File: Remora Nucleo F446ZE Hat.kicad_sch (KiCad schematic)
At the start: 16 parts, among them J1 NucleoF446ZE CN11 Header, J2 NucleoF446ZE CN12 Header, J3 UART_TX, J4 MSD-1-A

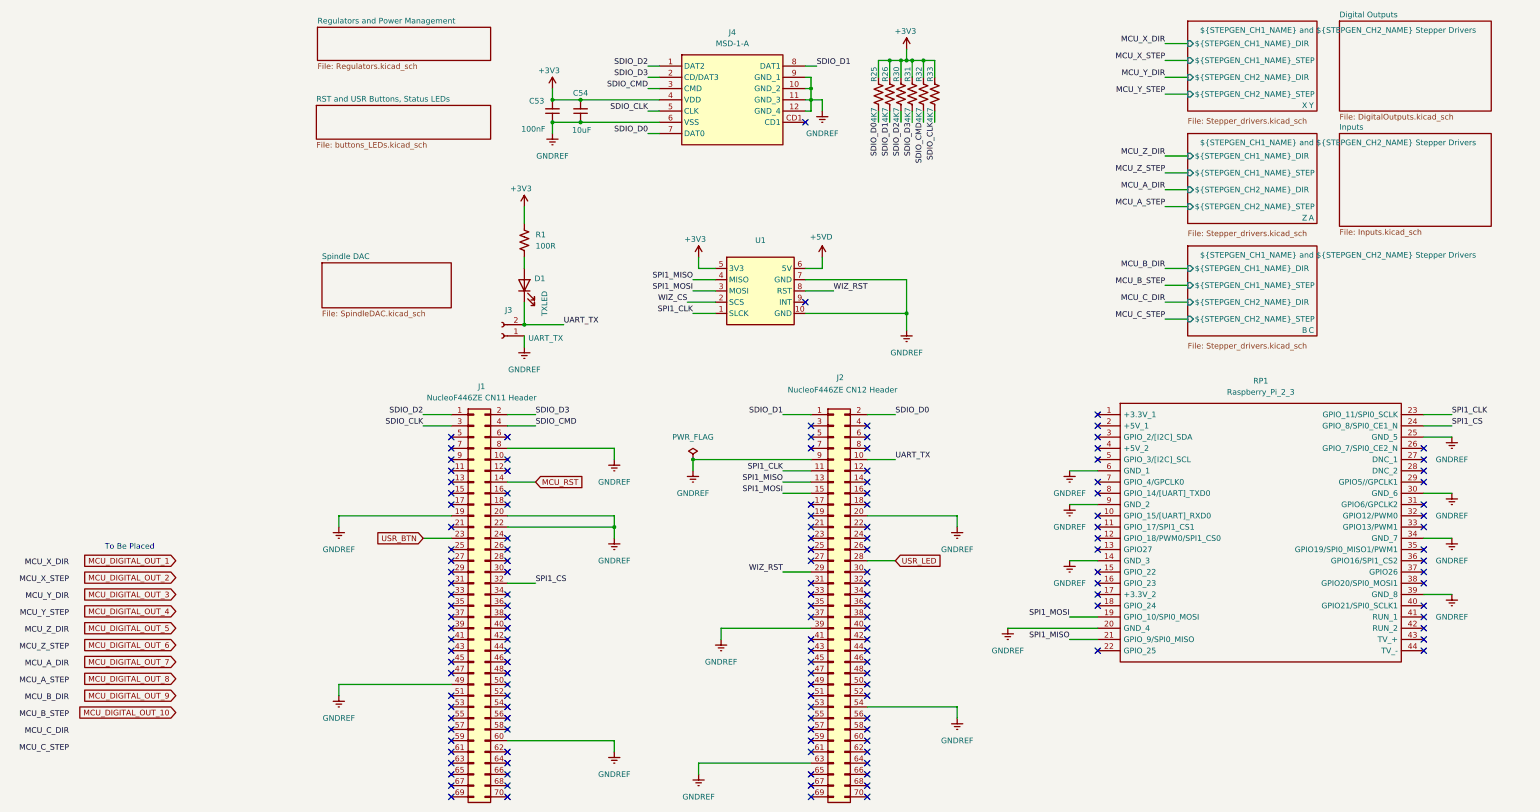
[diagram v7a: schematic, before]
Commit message: updates to read me, marked V1 parts inactive and made start on board layout for initial test board. fixes to BOM to suit
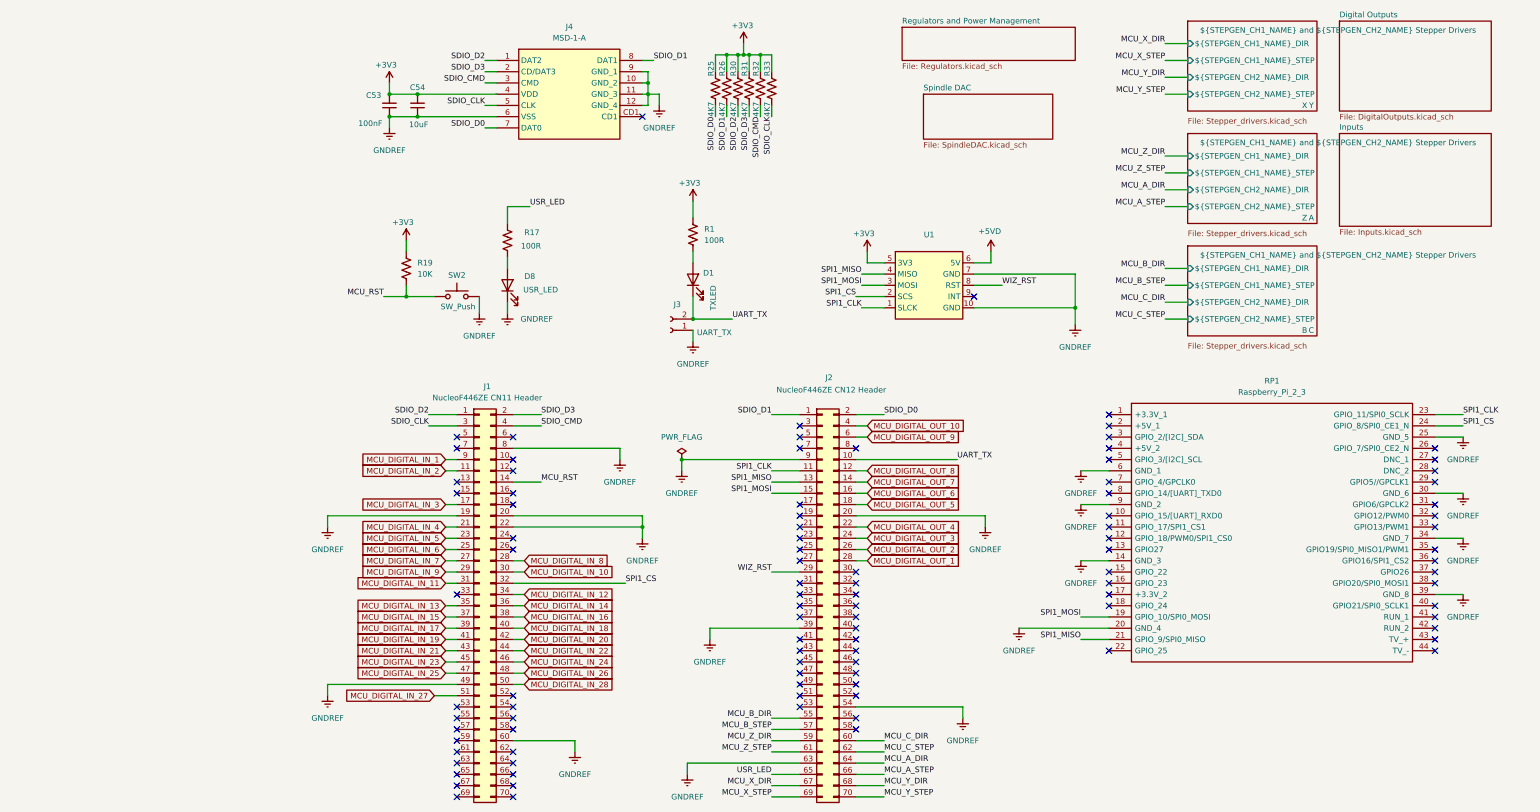
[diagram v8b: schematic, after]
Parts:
- added D8: USR_LED, Diode_SMD:D_1206_3216Metric_Pad1.42x1.75mm_HandSolder, symbol Device:LED
- added R17: 100R, Resistor_SMD:R_1206_3216Metric_Pad1.30x1.75mm_HandSolder, symbol Device:R_US
- added R19: 10K, Resistor_SMD:R_1206_3216Metric_Pad1.30x1.75mm_HandSolder, symbol Device:R_US
- added SW2: SW_Push, Button_Switch_SMD:SW_SPST_Omron_B3FS-100xP, symbol Switch:SW_Push
- J3: footprint EBWA_02_A:ADAMTECH_EBWA-02-A -> Connector_PinHeader_2.54mm:PinHeader_1x02_P2.54mm_Vertical
- RP1: footprint RPI3FootPrint:raspberrypi_2_3 -> RASPBERRYPI
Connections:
- net WIZ_CS is gone; now on net SPI1_CS: U1.2 (SCS)
- net +3V3: now also R19.1
- net GNDREF: now also D8.1 (K), SW2.2
- net MCU_A_DIR: now also J2.64 (Pin_64)
- net MCU_A_STEP: now also J2.66 (Pin_66)
- net MCU_B_DIR: now also J2.55 (Pin_55)
- net MCU_B_STEP: now also J2.57 (Pin_57)
- net MCU_C_DIR: now also J2.60 (Pin_60)
- net MCU_C_STEP: now also J2.62 (Pin_62)
- net MCU_DIGITAL_OUT_1: now also J2.28 (Pin_28)
- net MCU_DIGITAL_OUT_10: now also J2.4 (Pin_4)
- net MCU_DIGITAL_OUT_2: now also J2.26 (Pin_26)
- net MCU_DIGITAL_OUT_3: now also J2.24 (Pin_24)
- net MCU_DIGITAL_OUT_4: now also J2.22 (Pin_22)
- net MCU_DIGITAL_OUT_5: now also J2.18 (Pin_18)
- net MCU_DIGITAL_OUT_6: now also J2.16 (Pin_16)
- net MCU_DIGITAL_OUT_7: now also J2.14 (Pin_14)
- net MCU_DIGITAL_OUT_8: now also J2.12 (Pin_12)
- net MCU_DIGITAL_OUT_9: now also J2.6 (Pin_6)
- net MCU_RST: now also R19.2, SW2.1
- net MCU_X_DIR: now also J2.67 (Pin_67)
- net MCU_X_STEP: now also J2.69 (Pin_69)
- net MCU_Y_DIR: now also J2.68 (Pin_68)
- net MCU_Y_STEP: now also J2.70 (Pin_70)
- net MCU_Z_DIR: now also J2.59 (Pin_59)
- net MCU_Z_STEP: now also J2.61 (Pin_61)
- net USR_LED: now also J2.65 (Pin_65), R17.1; no longer J2.28 (Pin_28)
- net MCU_DIGITAL_IN_2: now reaches J1.11 (Pin_11)
- net MCU_DIGITAL_IN_3: now reaches J1.17 (Pin_17)
- net MCU_DIGITAL_IN_4: now reaches J1.21 (Pin_21)
- net MCU_DIGITAL_IN_6: now reaches J1.25 (Pin_25)
- net MCU_DIGITAL_IN_7: now reaches J1.27 (Pin_27)
- net MCU_DIGITAL_IN_8: now reaches J1.28 (Pin_28)
- net MCU_DIGITAL_IN_9: now reaches J1.29 (Pin_29)
- net MCU_DIGITAL_IN_10: now reaches J1.30 (Pin_30)
- net MCU_DIGITAL_IN_11: now reaches J1.31 (Pin_31)
- net MCU_DIGITAL_IN_12: now reaches J1.34 (Pin_34)
- net MCU_DIGITAL_IN_13: now reaches J1.35 (Pin_35)
- net MCU_DIGITAL_IN_14: now reaches J1.36 (Pin_36)
- net MCU_DIGITAL_IN_15: now reaches J1.37 (Pin_37)
- net MCU_DIGITAL_IN_16: now reaches J1.38 (Pin_38)
- net MCU_DIGITAL_IN_17: now reaches J1.39 (Pin_39)
- net MCU_DIGITAL_IN_18: now reaches J1.40 (Pin_40)
- net MCU_DIGITAL_IN_19: now reaches J1.41 (Pin_41)
- net MCU_DIGITAL_IN_20: now reaches J1.42 (Pin_42)
- net MCU_DIGITAL_IN_21: now reaches J1.43 (Pin_43)
- net MCU_DIGITAL_IN_22: now reaches J1.44 (Pin_44)
- net MCU_DIGITAL_IN_23: now reaches J1.45 (Pin_45)
- net MCU_DIGITAL_IN_24: now reaches J1.46 (Pin_46)
- net MCU_DIGITAL_IN_25: now reaches J1.47 (Pin_47)
- net MCU_DIGITAL_IN_26: now reaches J1.48 (Pin_48)
- net MCU_DIGITAL_IN_28: now reaches J1.50 (Pin_50)
- net MCU_DIGITAL_IN_27: now reaches J1.51 (Pin_51)
- net MCU_DIGITAL_IN_1: now reaches J1.9 (Pin_9)
- net USR_BTN renamed MCU_DIGITAL_IN_5
- new net: D8.2 (A), R17.2
- no-connect marks 148 -> 99
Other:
- removed sheet RST and USR Buttons, Status LEDs
- note removed: "To Be Placed"
- moved on the sheet: C53, C54, D1, J1, J2, J3, J4, R1, R25, R26, R30, R31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
